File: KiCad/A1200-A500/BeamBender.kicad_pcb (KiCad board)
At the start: 4 copper layers, 50 x 100 mm, 102 parts, among them J1 4-1734742-0, J2 HDMI_A_1.4, J3 STX-3501-3N, J4 Phoenix_Contact, J5 Conn_01x01, J6 Conn_02x06_Odd_Even, U1 LM1117-3.3, U2 GW1NR-UV9LQ144P, U3 ADV7513BSWZ, U4 MCP1702T-1802E_CB, U5 AK5720VT, X1 Abracon ASE-27.000MHZ-L-R-T, X2 5.0x3.2mm, X3 Oscillator_7.0x5.0mm

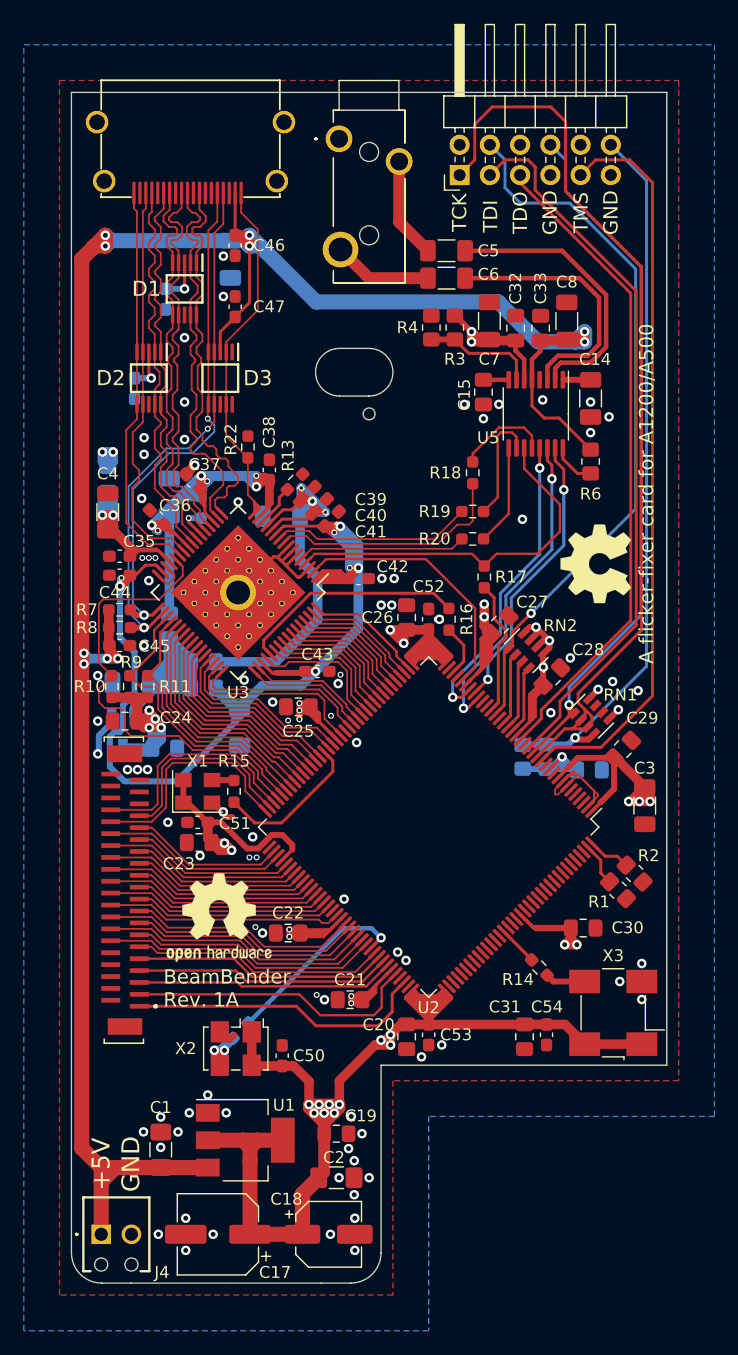
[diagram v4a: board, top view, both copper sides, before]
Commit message: Silkscreen fix
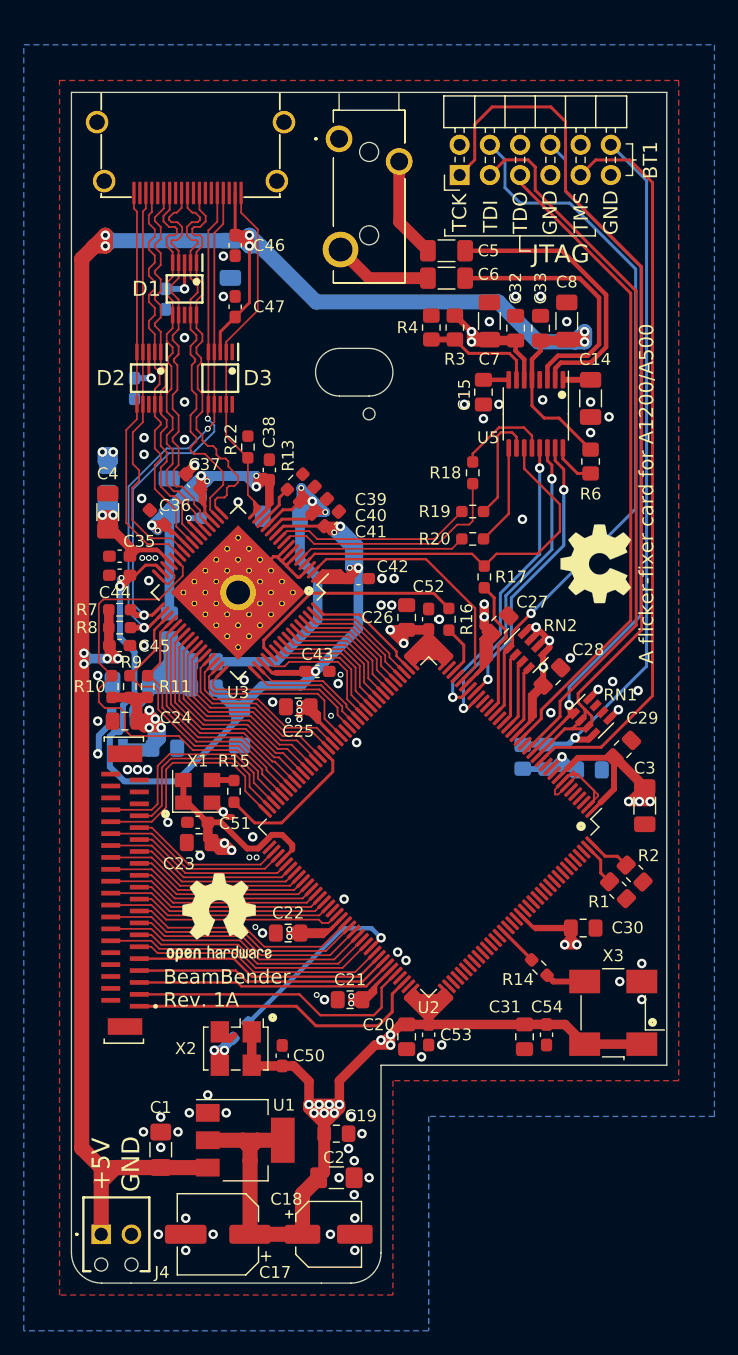
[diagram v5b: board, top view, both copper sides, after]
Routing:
- net GND: vias 84 -> 88
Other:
- board text added: "3V3"
- board text added: "BT1"
- board text added: "JP1"
- board text added: "JP2"
- board text added: "JTAG"

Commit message: small routing fix
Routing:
- net TCK: track 77.1 -> 76.4 mm

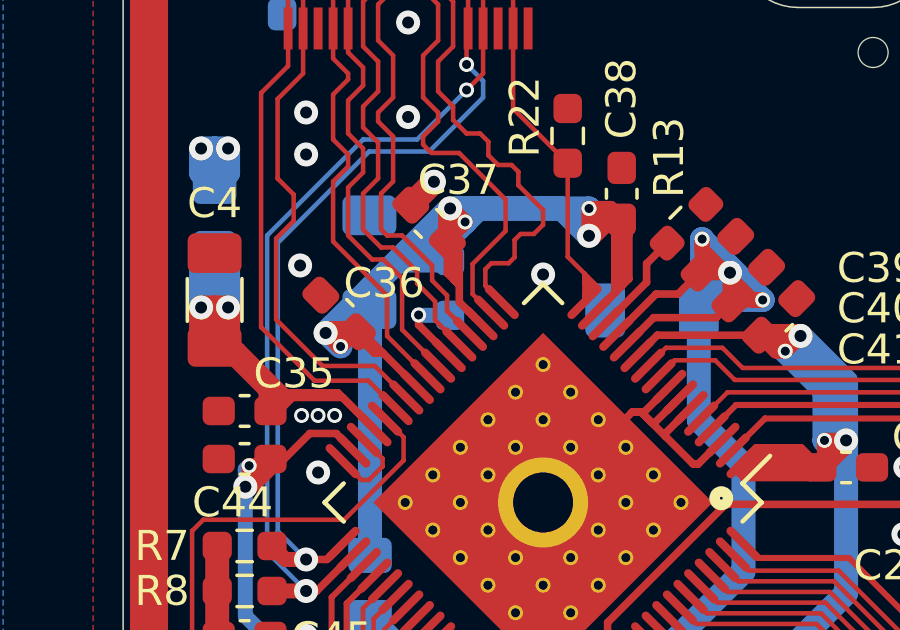
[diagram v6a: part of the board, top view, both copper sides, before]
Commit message: Changed R12 to a selectable pull-up/pull-down three-pads footprint
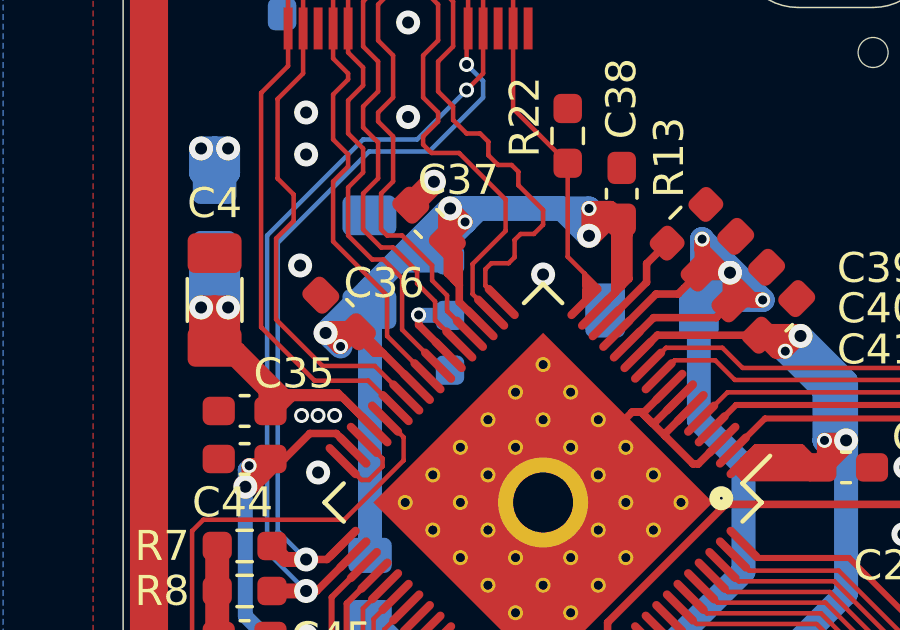
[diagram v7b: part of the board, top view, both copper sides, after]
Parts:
- R12: footprint Resistor_SMD:R_0603_1608Metric_Pad0.98x0.95mm_HandSolder -> BeamBender:ResistorJumper-3_Open_Pad_0603
- moved R12 0.93 mm to (109.0, 76.0)
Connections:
- R12 pad 1: /PD -> GND
- R12 pad 2: AVDD -> /PD
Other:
- board text added: "AVDD"

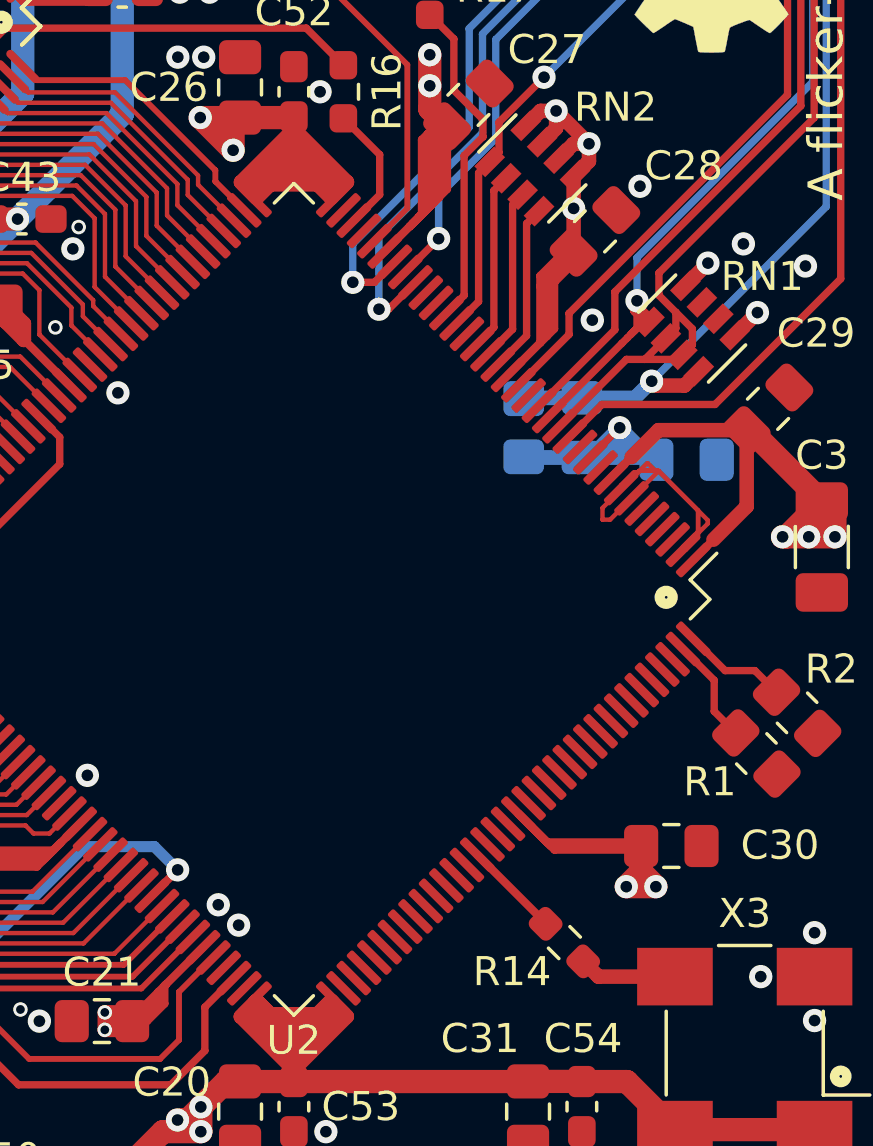
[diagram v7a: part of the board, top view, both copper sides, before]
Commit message: Added some GND via-stitching for the FPGA
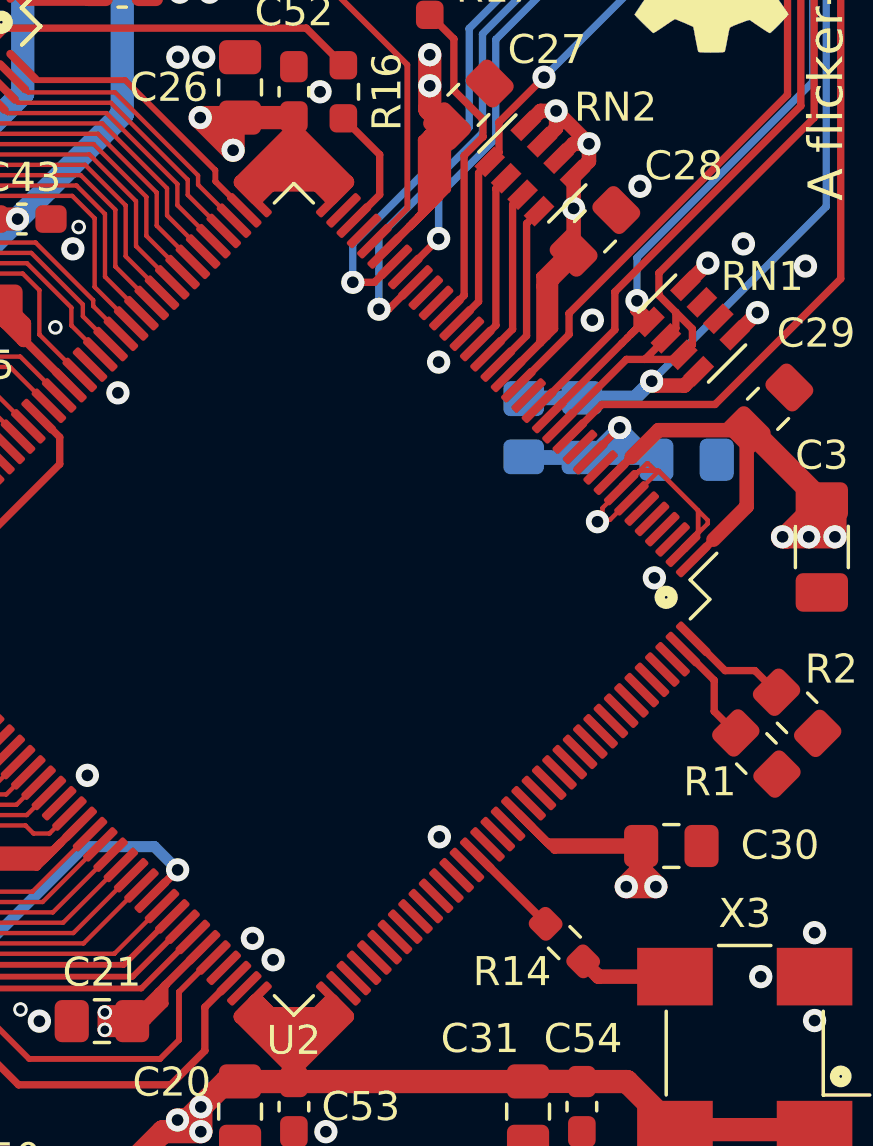
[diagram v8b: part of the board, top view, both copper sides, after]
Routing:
- net GND: vias 88 -> 92
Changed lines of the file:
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@@
     (thickness 1.6)
     (drawings 68)
-    (tracks 1808)
+    (tracks 1812)
     (zones 0)
     (modules 102)
@@
   (via (at 121.386 128.917) (size 0.8) (drill 0.4) (layers F.Cu B.Cu) (net 1))
   (via (at 121.611 126.217) (size 0.8) (drill 0.4) (layers F.Cu B.Cu) (net 1))
-  (via (at 126.211 113.117) (size 0.8) (drill 0.4) (layers F.Cu B.Cu) (net 1))
-  (via (at 125.511 112.417) (size 0.8) (drill 0.4) (layers F.Cu B.Cu) (net 1))
+  (via (at 126.686 113.5722) (size 0.8) (drill 0.4) (layers F.Cu B.Cu) (net 1))
+  (via (at 127.3972 114.3088) (size 0.8) (drill 0.4) (layers F.Cu B.Cu) (net 1))
   (via (at 106.211 101.517) (size 0.8) (drill 0.4) (layers F.Cu B.Cu) (net 1))
   (via (at 113.661 104.467) (size 0.5) (drill 0.3) (layers F.Cu B.Cu) (net 1))
@@
   (via (at 133.211 59.467) (size 0.8) (drill 0.4) (layers F.Cu B.Cu) (net 1))
   (via (at 139.711 59.467) (size 0.8) (drill 0.4) (layers F.Cu B.Cu) (net 1))
+  (via (at 133.111 110.0797) (size 0.8) (drill 0.4) (layers F.Cu B.Cu) (net 1))
+  (via (at 140.5036 101.177) (size 0.8) (drill 0.4) (layers F.Cu B.Cu) (net 1))
+  (via (at 138.5478 99.2466) (size 0.8) (drill 0.4) (layers F.Cu B.Cu) (net 1))
+  (via (at 133.0868 93.7602) (size 0.8) (drill 0.4) (layers F.Cu B.Cu) (net 1))
   (via (at 132.782 84.2606) (size 0.8) (drill 0.4) (layers F.Cu B.Cu) (net 2))
   (via (at 146.711 99.767) (size 0.8) (drill 0.4) (layers F.Cu B.Cu) (net 2))
@@
   (segment (start 104.611 62.017) (end 104.611 64.017) (width 0.254) (layer F.Cu) (net 83))
   (segment (start 104.811 64.217) (end 103.411 64.217) (width 0.5) (layer B.Cu) (net 83))
-  (segment (start 134.986237 92.566889) (end 134.413089 93.140037) (width 0.254) (layer F.Cu) (net 120))
-  (segment (start 134.986237 87.860393) (end 134.986237 92.566889) (width 0.254) (layer F.Cu) (net 120))
-  (segment (start 135.407878 87.438752) (end 134.986237 87.860393) (width 0.254) (layer F.Cu) (net 120))
+  (segment (start 135.0553 92.497826) (end 134.413089 93.140037) (width 0.254) (layer F.Cu) (net 120))
+  (segment (start 135.0553 87.79133) (end 135.0553 92.497826) (width 0.254) (layer F.Cu) (net 120))
+  (segment (start 135.407878 87.438752) (end 135.0553 87.79133) (width 0.254) (layer F.Cu) (net 120))
   (segment (start 135.630617 92.629616) (end 134.766643 93.49359) (width 0.254) (layer F.Cu) (net 121))
   (segment (start 135.630617 88.347383) (end 135.630617 92.629616) (width 0.254) (layer F.Cu) (net 121))
